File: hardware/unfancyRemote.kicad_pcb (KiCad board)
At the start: 2 copper layers, 30.5 x 61 mm, 33 parts, among them J1 Arduino Analog, J2 Arduino Digital, J3 HALL1, J4 HALL2, J5 PPM, J6 Conn_01x02, Q1 AO3401A, Q2 MMBT3904, SW1 SW_Push, U1 E28-2G4M12S

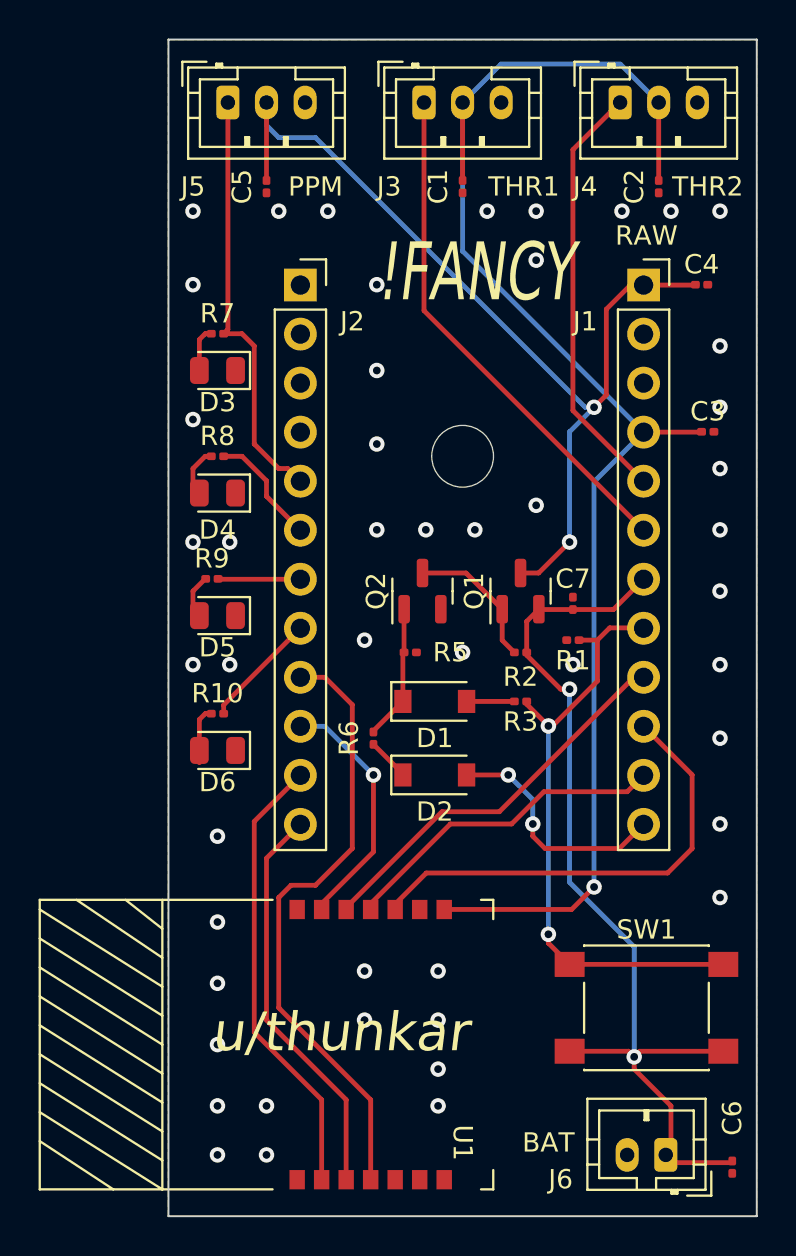
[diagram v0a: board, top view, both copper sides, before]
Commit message: Fixed R and Cs footprint
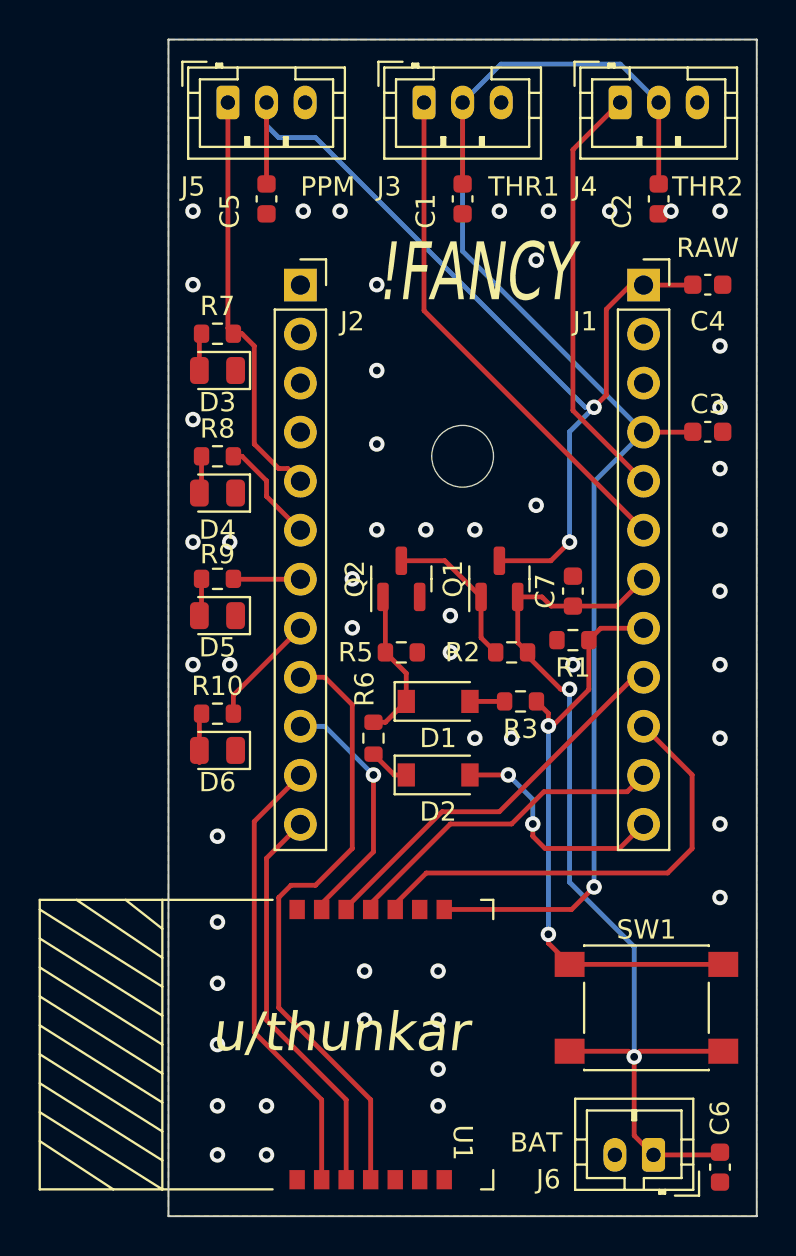
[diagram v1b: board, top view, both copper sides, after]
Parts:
- C1, C2, C3, C4, C5, C6, C7: footprint Capacitor_SMD:C_0201_0603Metric -> Capacitor_SMD:C_0603_1608Metric
- R1, R10, R2, R3, R5, R6, R7, R8, R9: footprint Resistor_SMD:R_0201_0603Metric -> Resistor_SMD:R_0603_1608Metric
- moved Q1 1.27 mm to (135.3, 87.6)
- moved Q2 1.27 mm to (130.2, 87.6)
- moved C7 0.64 mm to (139.1, 88.3)
- moved C1 0.63 mm to (133.3, 67.9)
- moved C2 0.63 mm to (143.5, 67.9)
- moved C5 0.63 mm to (123.2, 67.9)
- moved C6 0.63 mm to (146.7, 118.1)
- moved J6 0.63 mm to (143.2, 117.5)
- moved R2 0.46 mm to (135.9, 91.4)
- moved R5 0.46 mm to (130.2, 91.4)
- moved C4 0.32 mm to (146.1, 72.4)
- moved R9 0.29 mm to (120.7, 87.6)
- moved D1 0.17 mm to (132.1, 94.0)
- moved D2 0.17 mm to (132.1, 97.8)
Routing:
- net VBAT: track 50.0 -> 51.1 mm
- net Net-(D1-Pad1): track 7.02 -> 8.06 mm
- net L3: track 4.27 -> 3.48 mm
- net Net-(Q1-Pad1): track 7.41 -> 8.09 mm
- net Net-(D1-Pad2): track 2.47 -> 1.80 mm
- net Net-(D4-Pad2): track 2.62 -> 1.95 mm
- net Net-(D5-Pad2): track 2.50 -> 1.95 mm
- net L2: track 6.03 -> 5.53 mm
- net GND: vias 48 -> 52

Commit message: WIP 1.0
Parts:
- added  : MountingHole_3.2mm_M3_DIN965, MountingHole:MountingHole_3.2mm_M3_DIN965, F.Cu at (144.8, 103.5)
- added  : MountingHole_3.2mm_M3_DIN965, MountingHole:MountingHole_3.2mm_M3_DIN965, F.Cu at (121.3, 98.4)
- moved C6 12.0 mm to (136.5, 111.8), turned to 90 degrees
- moved D2 3.70 mm to (135.3, 95.9)
- moved D6 2.54 mm to (120.7, 94.0)
- moved R10 2.54 mm to (120.7, 92.1)
- moved R2 2.13 mm to (134.2, 90.2)
- moved C7 2.01 mm to (138.4, 86.4)
- moved Q2 2.01 mm to (130.8, 85.7)
- moved J2 1.92 mm to (126.4, 71.1)
- moved D4 1.91 mm to (120.7, 81.3)
- moved D5 1.91 mm to (120.7, 87.6)
- moved J6 1.91 mm to (145.1, 117.5)
- moved Q1 1.91 mm to (135.3, 85.7)
- moved R7 1.91 mm to (120.7, 73.0)
- moved R8 1.91 mm to (120.7, 79.4)
- moved R9 1.91 mm to (120.7, 85.7)
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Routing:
- net PPM: track 21.7 -> 0.00 mm
- net L4: track 5.86 -> 0.00 mm
- net L2: track 5.53 -> 0.00 mm
- net +3V3: track 76.3 -> 80.1 mm
- net L3: track 3.48 -> 0.00 mm
- net Net-(D6-Pad2): track 2.67 -> 0.00 mm
- net /RFBUSY: track 20.8 -> 23.5 mm
- net Net-(D5-Pad2): track 1.95 -> 0.00 mm
- net Net-(D4-Pad2): track 1.95 -> 0.00 mm
- net VBAT: track 51.1 -> 49.2 mm
- net /NRESET: track 23.4 -> 25.3 mm
- net Net-(D1-Pad1): track 8.06 -> 9.80 mm
- net HALL2: track 22.1 -> 20.4 mm
- net HALL1: track 26.9 -> 25.3 mm, vias 0 -> 1
- net Net-(D3-Pad2): track 2.03 -> 0.43 mm
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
